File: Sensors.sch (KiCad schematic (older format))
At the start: 46 parts, among them IC2 MAX11128ATI+, IC3 MAX11128ATI+, J5 Conn_01x02_Female, J6 Conn_01x02_Female, Q2 BSS138, Q3 BSS138, U2 REF3030

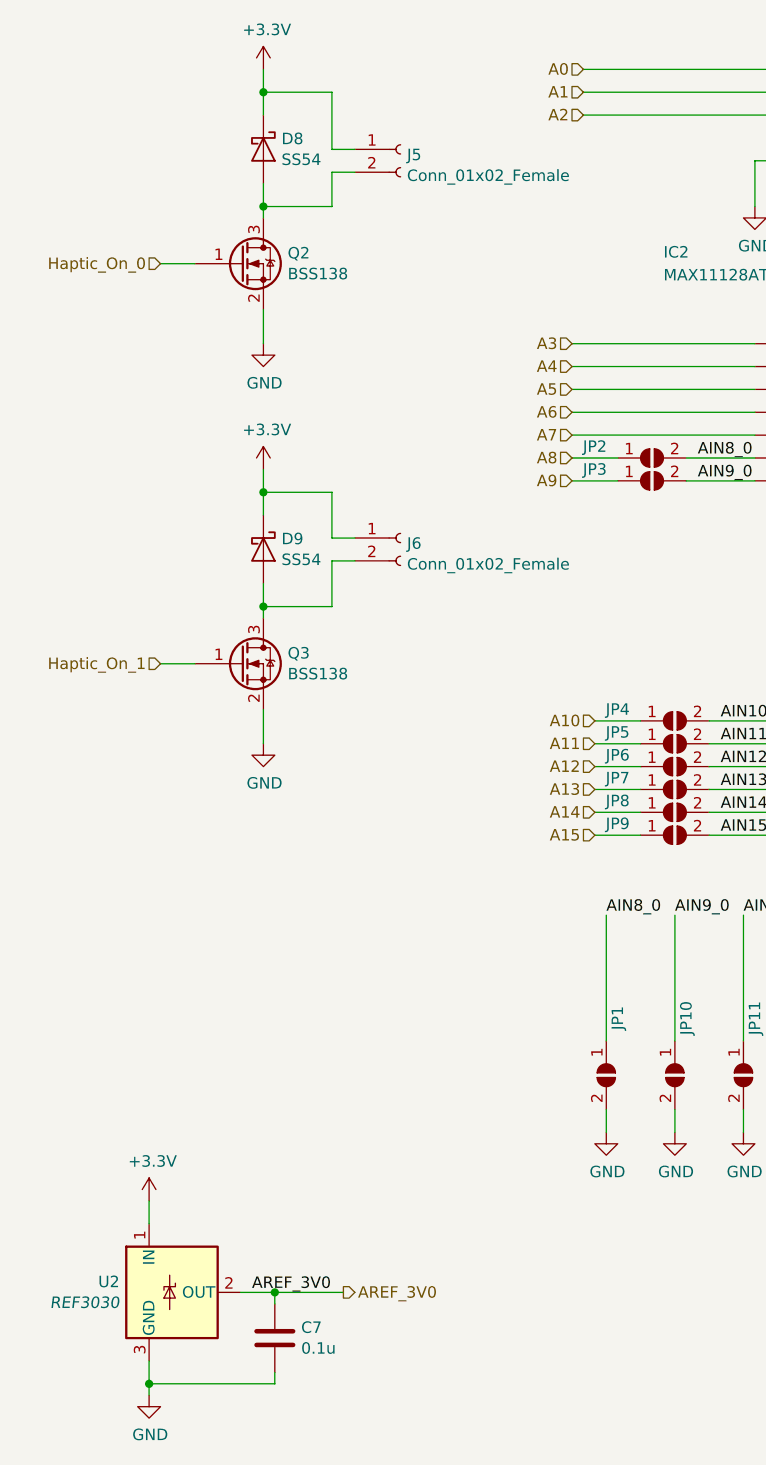
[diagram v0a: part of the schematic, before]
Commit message: Added project and digikey footprints. Added mini-spox connectors.
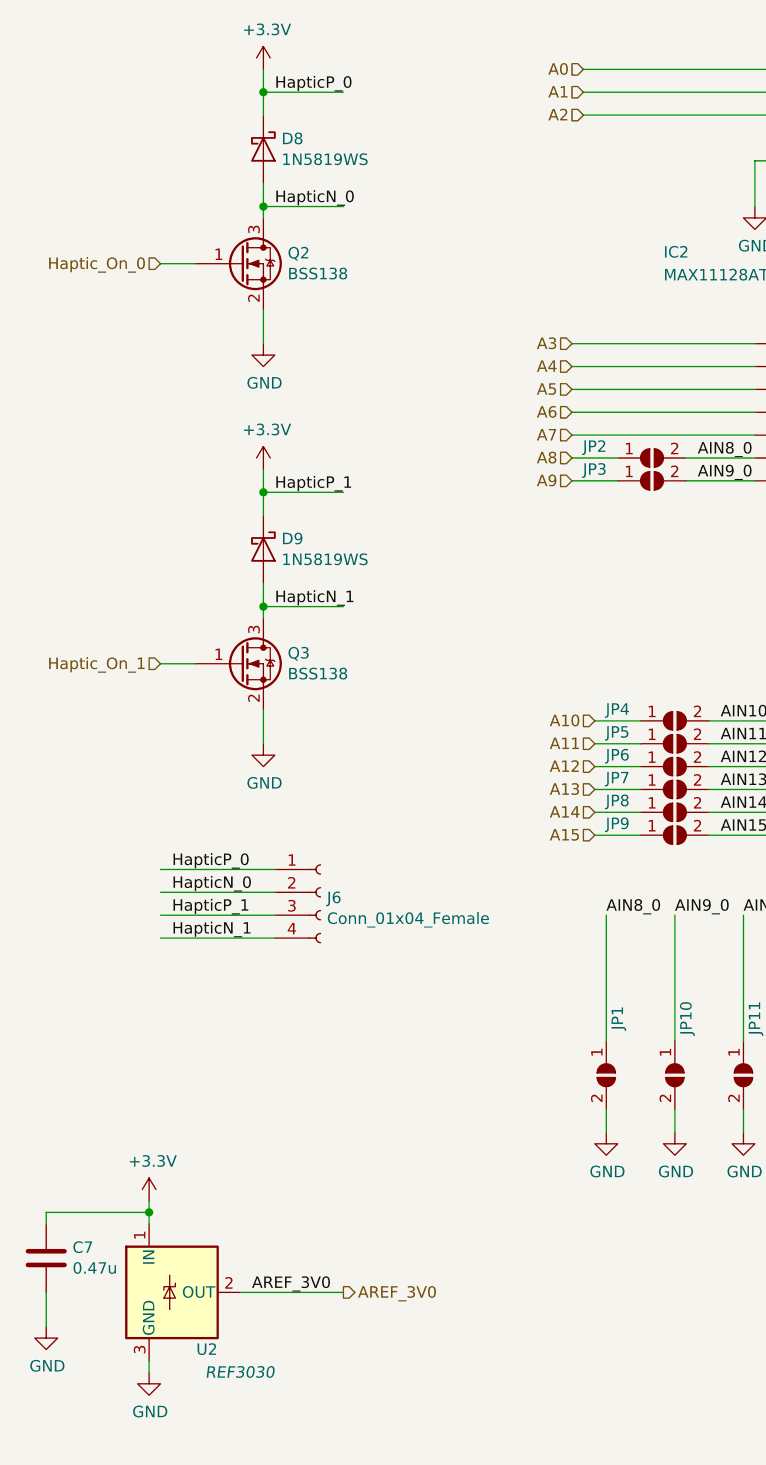
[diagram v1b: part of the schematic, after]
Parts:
- removed J5, J6: Conn_01x02_Female, Connector_JST:JST_PH_B2B-PH-SM4-TB_1x02_P2.00mm_Vertical, symbol Connector:Conn_01x02_Female
- added J6: Conn_01x04_Female, Glove-PCB:22-05-7045, symbol Connector:Conn_01x04_Female
- C7: value 0.1u -> 0.47u
- D8, D9: value SS54 -> 1N5819WS; footprint Diode_SMD:D_SMA_Handsoldering -> Diode_SMD:D_SOD-323
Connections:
- net labels added: HapticN_0, HapticN_1, HapticP_0, HapticP_1
- wire segments 190 -> 185
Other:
- moved on the sheet: C7
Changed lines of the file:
@@
 L Device:C C7
 U 1 1 5FB6FE47
-P 1800 7000
-F 0 "C7" H 1915 7046 50  0000 L CNN
-F 1 "0.1u" H 1915 6955 50  0000 L CNN
-F 2 "Capacitors_SMD:C_0603_HandSoldering" H 1838 6850 50  0001 C CNN
-F 3 "~" H 1800 7000 50  0001 C CNN
-	1    1800 7000
-	1    0    0    -1
-$EndComp
-Wire Wire Line
-	1800 6850 1800 6800
+P 800 6650
+F 0 "C7" H 915 6696 50  0000 L CNN
+F 1 "0.47u" H 915 6605 50  0000 L CNN
+F 2 "Capacitors_SMD:C_0603_HandSoldering" H 838 6500 50  0001 C CNN
+F 3 "~" H 800 6650 50  0001 C CNN
+	1    800  6650
+	1    0    0    -1
+$EndComp
 $Comp
 L Device:C C8
@@
 AIN8_0
 $Comp
-L Jumper:SolderJumper_2_Open JP2
-U 1 1 5FBC7681
-P 3450 3150
-F 0 "JP2" H 3200 3200 50  0000 C CNN
-F 1 "SolderJumper_2_Open" H 3450 3264 50  0001 C CNN
-F 2 "Jumper:SolderJumper-2_P1.3mm_Open_RoundedPad1.0x1.5mm" H 3450 3150 50  0001 C CNN
-F 3 "~" H 3450 3150 50  0001 C CNN
-	1    3450 3150
-	1    0    0    -1
-$EndComp
-$Comp
-L Jumper:SolderJumper_2_Open JP3
-U 1 1 5FBC8295
-P 3450 3250
-F 0 "JP3" H 3200 3300 50  0000 C CNN
-F 1 "SolderJumper_2_Open" H 3450 3364 50  0001 C CNN
-F 2 "Jumper:SolderJumper-2_P1.3mm_Open_RoundedPad1.0x1.5mm" H 3450 3250 50  0001 C CNN
-F 3 "~" H 3450 3250 50  0001 C CNN
-	1    3450 3250
-	1    0    0    -1
-$EndComp
-$Comp
 L Jumper:SolderJumper_2_Open JP4
 U 1 1 5FBC88C5
@@
 U 1 1 5FC13A13
 P 1350 6800
-F 0 "U2" H 1121 6846 50  0000 R CNN
-F 1 "REF3030" H 1121 6755 50  0000 R CIN
+F 0 "U2" H 1550 6550 50  0000 R CNN
+F 1 "REF3030" H 1800 6450 50  0000 R CIN
 F 2 "Package_TO_SOT_SMD:SOT-23" H 1350 6350 50  0001 C CIN
 F 3 "http://www.ti.com/lit/ds/symlink/ref3033.pdf" H 1450 6450 50  0001 C CIN
@@
 	1    0    0    -1
 $EndComp
-Wire Wire Line
-	1650 6800 1800 6800
 Text Label 1700 6800 0    50   ~ 0
 AREF_3V0
@@
 $EndComp
 Wire Wire Line
-	1250 6400 1250 6500
+	1250 6400 1250 6450
 $Comp
 L SamacSys_Parts:MAX11128ATI+ IC3
@@
 	0    1    1    0
 $EndComp
-Connection ~ 1250 7200
-Wire Wire Line
-	1800 7200 1250 7200
 $Comp
 L power:GND #PWR034
 U 1 1 5FB5CB7F
-P 1250 7250
-F 0 "#PWR034" H 1250 7000 50  0001 C CNN
-F 1 "GND" H 1255 7077 50  0000 C CNN
-F 2 "" H 1250 7250 50  0001 C CNN
-F 3 "" H 1250 7250 50  0001 C CNN
-	1    1250 7250
-	1    0    0    -1
-$EndComp
-Wire Wire Line
-	1250 7200 1250 7250
-Wire Wire Line
-	1250 7100 1250 7200
-Wire Wire Line
-	1800 7150 1800 7200
+P 1250 7150
+F 0 "#PWR034" H 1250 6900 50  0001 C CNN
+F 1 "GND" H 1255 6977 50  0000 C CNN
+F 2 "" H 1250 7150 50  0001 C CNN
+F 3 "" H 1250 7150 50  0001 C CNN
+	1    1250 7150
+	1    0    0    -1
+$EndComp
 Wire Wire Line
 	5300 2950 6100 2950
@@
 Wire Wire Line
 	1750 3700 1750 3800
-Wire Wire Line
-	2050 3800 1750 3800
 Connection ~ 1750 3800
 Wire Wire Line
@@
 Wire Wire Line
 	1750 3200 1750 3300
-Wire Wire Line
-	2050 3300 1750 3300
 Connection ~ 1750 3300
 Wire Wire Line
@@
 AR Path="/5FBB3CB1/5FEE0924" Ref="D8"  Part="1"
 F 0 "D8" V 1704 1879 50  0000 L CNN
-F 1 "SS54" V 1795 1879 50  0000 L CNN
-F 2 "Diode_SMD:D_SMA_Handsoldering" H 1750 1800 50  0001 C CNN
+F 1 "1N5819WS" V 1795 1879 50  0000 L CNN
+F 2 "Diode_SMD:D_SOD-323" H 1750 1800 50  0001 C CNN
 F 3 "https://datasheet.lcsc.com/szlcsc/1903061001_MDD-Jiangsu-Yutai-Elec-SS54_C22452.pdf" H 1750 1800 50  0001 C CNN
 	1    1750 1800
@@
 AR Path="/5FBB3CB1/5FEE8F49" Ref="D9"  Part="1"
 F 0 "D9" V 1704 3629 50  0000 L CNN
-F 1 "SS54" V 1795 3629 50  0000 L CNN
-F 2 "Diode_SMD:D_SMA_Handsoldering" H 1750 3550 50  0001 C CNN
+F 1 "1N5819WS" V 1795 3629 50  0000 L CNN
+F 2 "Diode_SMD:D_SOD-323" H 1750 3550 50  0001 C CNN
 F 3 "https://datasheet.lcsc.com/szlcsc/1903061001_MDD-Jiangsu-Yutai-Elec-SS54_C22452.pdf" H 1750 3550 50  0001 C CNN
 	1    1750 3550
 	0    1    1    0
 $EndComp
-$Comp
-L Connector:Conn_01x02_Female J?
-U 1 1 5FF0B55C
-P 2350 1800
-AR Path="/5FB48E27/5FF0B55C" Ref="J?"  Part="1"
-AR Path="/5FBB3CB1/5FF0B55C" Ref="J5"  Part="1"
-F 0 "J5" H 2378 1776 50  0000 L CNN
-F 1 "Conn_01x02_Female" H 2378 1685 50  0000 L CNN
-F 2 "Connector_JST:JST_PH_B2B-PH-SM4-TB_1x02_P2.00mm_Vertical" H 2350 1800 50  0001 C CNN
-F 3 "http://www.jst.com/home8.html" H 2350 1800 50  0001 C CNN
-	1    2350 1800
-	1    0    0    -1
-$EndComp
-$Comp
-L Connector:Conn_01x02_Female J?
-U 1 1 5FF13E92
-P 2350 3500
-AR Path="/5FB48E27/5FF13E92" Ref="J?"  Part="1"
-AR Path="/5FBB3CB1/5FF13E92" Ref="J6"  Part="1"
-F 0 "J6" H 2378 3476 50  0000 L CNN
-F 1 "Conn_01x02_Female" H 2378 3385 50  0000 L CNN
-F 2 "Connector_JST:JST_PH_B2B-PH-SM4-TB_1x02_P2.00mm_Vertical" H 2350 3500 50  0001 C CNN
-F 3 "http://www.jst.com/home8.html" H 2350 3500 50  0001 C CNN
-	1    2350 3500
-	1    0    0    -1
-$EndComp
-Wire Wire Line
-	2050 3300 2050 3500
-Wire Wire Line
-	2050 3500 2150 3500
-Wire Wire Line
-	2150 3600 2050 3600
-Wire Wire Line
-	2050 3600 2050 3800
-Wire Wire Line
-	1750 2050 2050 2050
-Wire Wire Line
-	2050 2050 2050 1900
-Wire Wire Line
-	2050 1900 2150 1900
-Wire Wire Line
-	2150 1800 2050 1800
-Wire Wire Line
-	2050 1800 2050 1550
-Wire Wire Line
-	1750 1550 2050 1550
-Wire Wire Line
-	1800 6800 2100 6800
-Connection ~ 1800 6800
 Text HLabel 2100 6800 2    50   Output ~ 0
 AREF_3V0
+Wire Wire Line
+	1750 3300 2100 3300
+Wire Wire Line
+	1750 3800 2100 3800
+Text Label 1800 1550 0    50   ~ 0
+HapticP_0
+Text Label 1800 2050 0    50   ~ 0
+HapticN_0
+Text Label 1800 3300 0    50   ~ 0
+HapticP_1
+Text Label 1800 3800 0    50   ~ 0
+HapticN_1
+Wire Wire Line
+	1750 2050 2100 2050
+Wire Wire Line
+	1750 1550 2100 1550
+$Comp
+L Connector:Conn_01x04_Female J?
+U 1 1 5FCB7BF1
+P 2000 5050
+AR Path="/5FCB7BF1" Ref="J?"  Part="1"
+AR Path="/5FBB3CB1/5FCB7BF1" Ref="J6"  Part="1"
+F 0 "J6" H 2028 5026 50  0000 L CNN
+F 1 "Conn_01x04_Female" H 2028 4935 50  0000 L CNN
+F 2 "Glove-PCB:22-05-7045" H 2000 5050 50  0001 C CNN
+F 3 "~" H 2000 5050 50  0001 C CNN
+	1    2000 5050
+	1    0    0    -1
+$EndComp
+Wire Wire Line
+	1800 4950 1300 4950
+Wire Wire Line
+	1300 5250 1800 5250
+Wire Wire Line
+	1800 5150 1300 5150
+Wire Wire Line
+	1800 5050 1300 5050
+Text Label 1350 5250 0    50   ~ 0
+HapticN_1
+Text Label 1350 5150 0    50   ~ 0
+HapticP_1
+Text Label 1350 5050 0    50   ~ 0
+HapticN_0
+Text Label 1350 4950 0    50   ~ 0
+HapticP_0
+Wire Wire Line
+	1250 7100 1250 7150
+$Comp
+L power:GND #PWR0101
+U 1 1 5FC4070C
+P 800 6950
+F 0 "#PWR0101" H 800 6700 50  0001 C CNN
+F 1 "GND" H 805 6777 50  0000 C CNN
+F 2 "" H 800 6950 50  0001 C CNN
+F 3 "" H 800 6950 50  0001 C CNN
+	1    800  6950
+	1    0    0    -1
+$EndComp
+Wire Wire Line
+	800  6800 800  6950
+Wire Wire Line
+	800  6500 800  6450
+Wire Wire Line
+	800  6450 1250 6450
+Connection ~ 1250 6450
+Wire Wire Line
+	1250 6450 1250 6500
+Wire Wire Line
+	1650 6800 2100 6800
+$Comp
+L Jumper:SolderJumper_2_Open JP3
+U 1 1 5FBC8295
+P 3450 3250
+F 0 "JP3" H 3200 3300 50  0000 C CNN
+F 1 "SolderJumper_2_Open" H 3450 3364 50  0001 C CNN
+F 2 "Jumper:SolderJumper-2_P1.3mm_Open_RoundedPad1.0x1.5mm" H 3450 3250 50  0001 C CNN
+F 3 "~" H 3450 3250 50  0001 C CNN
+	1    3450 3250
+	1    0    0    -1
+$EndComp
+$Comp
+L Jumper:SolderJumper_2_Open JP2
+U 1 1 5FBC7681
+P 3450 3150
+F 0 "JP2" H 3200 3200 50  0000 C CNN
+F 1 "SolderJumper_2_Open" H 3450 3264 50  0001 C CNN
+F 2 "Jumper:SolderJumper-2_P1.3mm_Open_RoundedPad1.0x1.5mm" H 3450 3150 50  0001 C CNN
+F 3 "~" H 3450 3150 50  0001 C CNN
+	1    3450 3150
+	1    0    0    -1
+$EndComp
 $EndSCHEMATC

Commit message: Placement done. Started layout.
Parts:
- removed JP1, JP10, JP11, JP12, JP13, JP14, JP15, JP16, JP17, JP18, JP19, JP2, JP20, JP21, JP22, JP23, JP24, JP25, JP26, JP27, JP28, JP29, JP3, JP30, JP31, JP32, JP4, JP5, JP6, JP7, JP8, JP9: SolderJumper_2_Open, Jumper:SolderJumper-2_P1.3mm_Open_RoundedPad1.0x1.5mm, symbol Jumper:SolderJumper_2_Open
- added C13, C15: 0.1u, Capacitors_SMD:C_0603_HandSoldering, symbol Device:C
- added C14, C16: 10u, Capacitors_SMD:C_0603_HandSoldering, symbol Device:C
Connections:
- net labels removed: AIN10_0, AIN10_1, AIN11_0, AIN11_1, AIN12_0, AIN12_1, AIN13_0, AIN13_1, AIN14_0, AIN14_1, AIN15_0, AIN15_1, AIN8_0, AIN8_1, AIN9_0, AIN9_1
- wire segments 185 -> 149
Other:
- moved on the sheet: C10, C11
